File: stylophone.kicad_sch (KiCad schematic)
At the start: 8 parts, among them U1 LM555xM

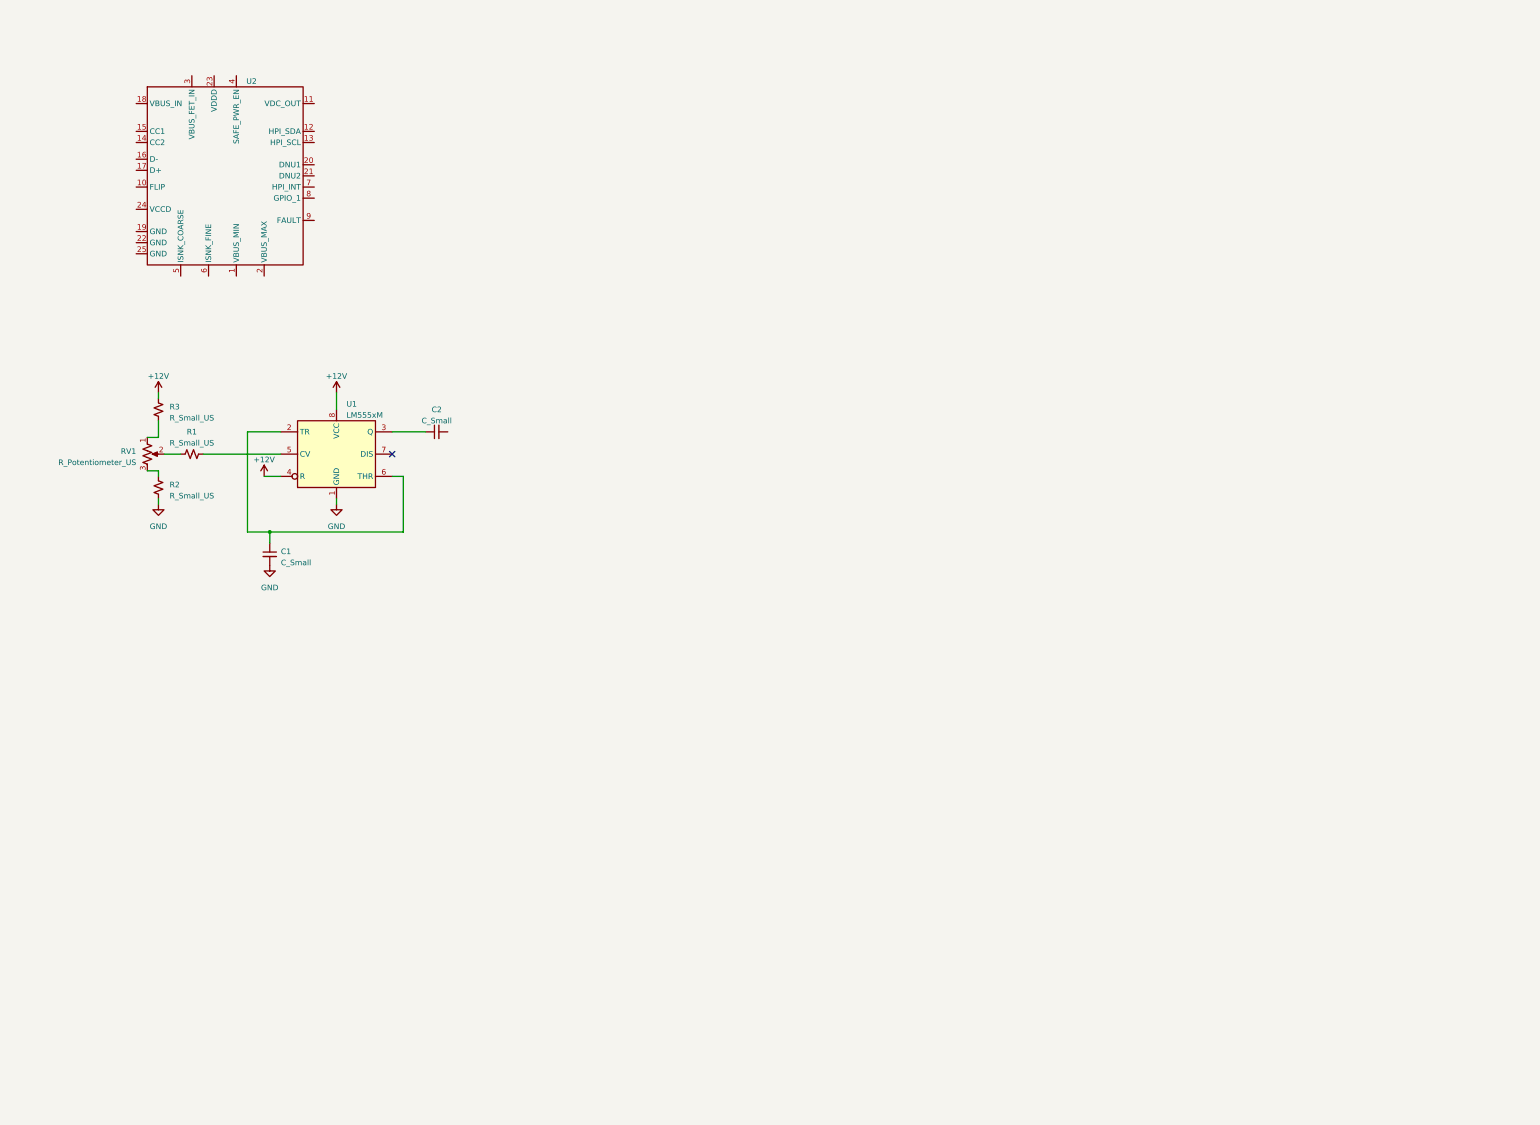
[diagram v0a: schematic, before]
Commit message: Updated all values and footprints
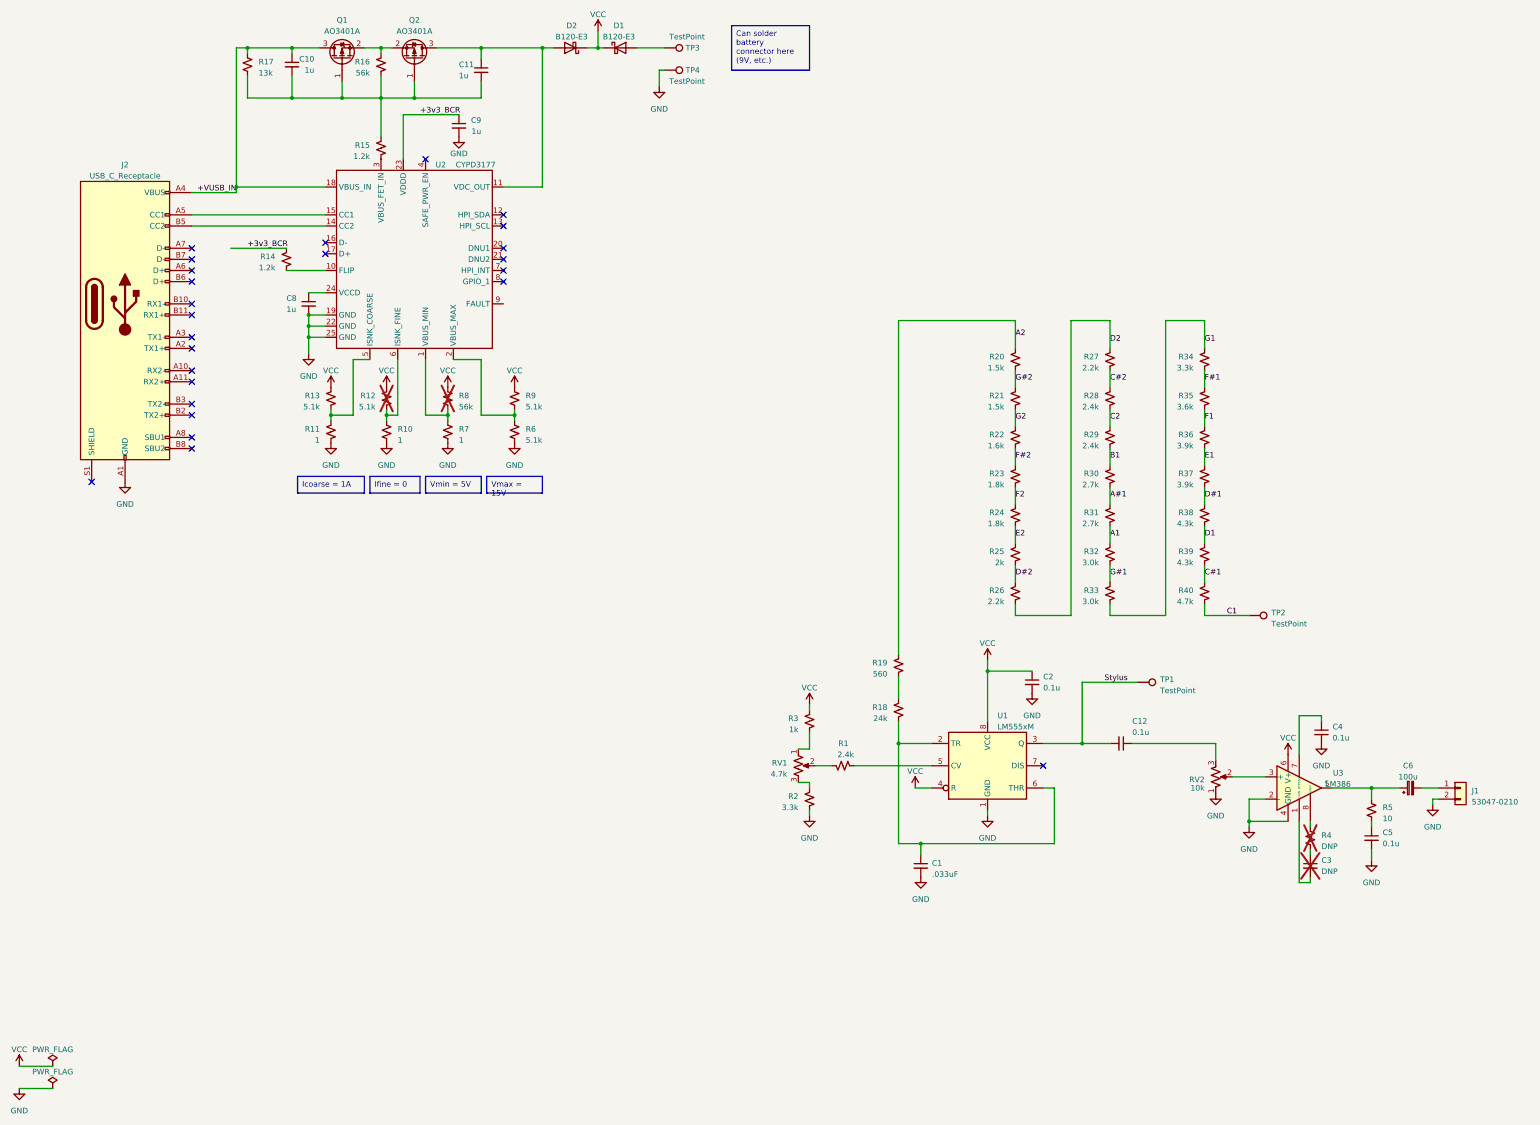
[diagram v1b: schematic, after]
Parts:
- added C10, C11, C8, C9: 1u, Capacitor_SMD:C_0603_1608Metric, symbol Device:C_Small
- added C12, C4, C5: 0.1u, Capacitor_SMD:C_0603_1608Metric, symbol Device:C_Small
- added C3: DNP, Capacitor_SMD:C_0603_1608Metric, symbol Device:C_Small
- added C6: 100u, Capacitor_SMD:CP_Elec_8x6.2, symbol Device:C_Polarized_Small
- added D1, D2: B120-E3, Diode_SMD:D_SMA, symbol Diode:B120-E3
- added J1: 53047-0210, Connector_Molex:Molex_PicoBlade_53047-0210_1x02_P1.25mm_Vertical, symbol Connector_Generic:Conn_01x02
- added J2: USB_C_Receptacle, Connector_USB:USB_C_Receptacle_Molex_105450-0101, symbol Connector:USB_C_Receptacle
- added Q1, Q2: AO3401A, Package_TO_SOT_SMD:SOT-23, symbol Transistor_FET:AO3401A
- added R10, R11, R7: 1, Resistor_SMD:R_0603_1608Metric, symbol Device:R_Small_US
- added R12, R13, R6, R9: 5.1k, Resistor_SMD:R_0603_1608Metric, symbol Device:R_Small_US
- added R14, R15: 1.2k, Resistor_SMD:R_0603_1608Metric, symbol Device:R_Small_US
- added R16, R8: 56k, Resistor_SMD:R_0603_1608Metric, symbol Device:R_Small_US
- added R17: 13k, Resistor_SMD:R_0603_1608Metric, symbol Device:R_Small_US
- added R18: 24k, Resistor_SMD:R_0603_1608Metric, symbol Device:R_Small_US
- added R19: 560, Resistor_SMD:R_0603_1608Metric, symbol Device:R_Small_US
- added R20, R21: 1.5k, Resistor_SMD:R_0603_1608Metric, symbol Device:R_Small_US
- added R22: 1.6k, Resistor_SMD:R_0603_1608Metric, symbol Device:R_Small_US
- added R23, R24: 1.8k, Resistor_SMD:R_0603_1608Metric, symbol Device:R_Small_US
- added R25: 2k, Resistor_SMD:R_0603_1608Metric, symbol Device:R_Small_US
- added R26, R27: 2.2k, Resistor_SMD:R_0603_1608Metric, symbol Device:R_Small_US
- added R28, R29: 2.4k, Resistor_SMD:R_0603_1608Metric, symbol Device:R_Small_US
- added R30, R31: 2.7k, Resistor_SMD:R_0603_1608Metric, symbol Device:R_Small_US
- added R32, R33: 3.0k, Resistor_SMD:R_0603_1608Metric, symbol Device:R_Small_US
- added R34: 3.3k, Resistor_SMD:R_0603_1608Metric, symbol Device:R_Small_US
- added R35: 3.6k, Resistor_SMD:R_0603_1608Metric, symbol Device:R_Small_US
- added R36, R37: 3.9k, Resistor_SMD:R_0603_1608Metric, symbol Device:R_Small_US
- added R38, R39: 4.3k, Resistor_SMD:R_0603_1608Metric, symbol Device:R_Small_US
- added R4: DNP, Resistor_SMD:R_0603_1608Metric, symbol Device:R_Small_US
- added R40: 4.7k, Resistor_SMD:R_0603_1608Metric, symbol Device:R_Small_US
- added R5: 10, Resistor_SMD:R_0603_1608Metric, symbol Device:R_Small_US
- added RV2: 10k, Potentiometer_THT:Potentiometer_Piher_T-16H_Single_Horizontal, symbol Device:R_Potentiometer_US
- added TP1, TP2, TP3, TP4: TestPoint, TestPoint:TestPoint_THTPad_D1.5mm_Drill0.7mm, symbol Connector:TestPoint
- added U3: LM386, Package_SO:SOIC-8_3.9x4.9mm_P1.27mm, symbol Amplifier_Audio:LM386
- C1: value C_Small -> .033uF
- C2: value C_Small -> 0.1u; footprint (none) -> Capacitor_SMD:C_0603_1608Metric
- R1: value R_Small_US -> 2.4k; footprint (none) -> Resistor_SMD:R_0603_1608Metric
- R2: value R_Small_US -> 3.3k; footprint (none) -> Resistor_SMD:R_0603_1608Metric
- R3: value R_Small_US -> 1k; footprint (none) -> Resistor_SMD:R_0603_1608Metric
- RV1: value R_Potentiometer_US -> 4.7k; footprint (none) -> Potentiometer_THT:Potentiometer_Piher_T-16H_Single_Horizontal
- U2: value ~ -> CYPD3177; footprint (none) -> Package_DFN_QFN:QFN-24-1EP_4x4mm_P0.5mm_EP2.15x2.15mm
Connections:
- net GND: now also C2.2, U2.19 (GND), U2.22 (GND), U2.25 (GND), C4.2, C5.2, C8.2, C9.2, J1.2 (Pin_2), J2.A1 (GND), J2.A12 (GND), J2.B1 (GND), J2.B12 (GND), R10.1, R11.1, R6.1, R7.1, RV2.1, TP4.1, U3.2 (-), U3.4 (GND)
- net at RV1.2: now also R1.2; no longer R1.1
- net at C1.1, U1.2 (TR), U1.6 (THR): now also R18.1
- net at U2.1 (VBUS_MIN): now also R7.2, R8.1
- net at U2.10 (FLIP): now also R14.1
- net at U2.11 (VDC_OUT): now also C11.1, D2.2 (A), Q2.3 (D)
- net at U2.14 (CC2): now also J2.B5 (CC2)
- net at U2.15 (CC1): now also J2.A5 (CC1)
- net +VUSB_IN: now reaches U2.18 (VBUS_IN)
- net +VUSB_IN: now also C10.1, J2.A4 (VBUS), J2.A9 (VBUS), J2.B4 (VBUS), J2.B9 (VBUS), Q1.3 (D), R17.2
- net at U2.2 (VBUS_MAX): now also R6.2, R9.1
- net +3v3_BCR: now reaches U2.23 (VDDD)
- net +3v3_BCR: now also C9.1, R14.2
- net at U2.24 (VCCD): now also C8.1
- net at U2.3 (VBUS_FET_IN): now also R15.1
- net at U2.5 (ISNK_COARSE): now also R11.2, R13.1
- net at U2.6 (ISNK_FINE): now also R10.2, R12.1
- net at U1.5 (CV): now also R1.1; no longer R1.2
- net Stylus: now reaches U1.3 (Q)
- net Stylus: now also C12.2, TP1.1; no longer C2.1
- net +12V renamed VCC
- net VCC: now also C2.1, D1.1 (K), D2.1 (K), R12.2, R13.2, R8.2, R9.2, U3.6 (V+)
- new net: C12.1, RV2.3
- new net: C3.1, R4.1
- new net: C3.2, U3.1 (GAIN)
- new net: D1.2 (A), TP3.1
- new net: C10.2, C11.2, Q1.1 (G), Q2.1 (G), R15.2, R16.1, R17.1
- new net: Q1.2 (S), Q2.2 (S), R16.2
- new net: R4.2, U3.8 (GAIN)
- new net: RV2.2, U3.3 (+)
- new net: C6.1, R5.2, U3.5
- new net: C4.1, U3.7 (BYPASS)
- new net: R18.2, R19.1
- new net: C5.1, R5.1
- new net: C6.2, J1.1 (Pin_1)
- new net A#1: R30.1, R31.2
- new net A1: R31.1, R32.2
- new net A2: R19.2, R20.2
- new net B1: R29.1, R30.2
- new net C#1: R39.1, R40.2
- new net C#2: R27.1, R28.2
- new net C1: R40.1, TP2.1
- new net C2: R28.1, R29.2
- new net D#1: R37.1, R38.2
- new net D#2: R25.1, R26.2
- new net D1: R38.1, R39.2
- new net D2: R26.1, R27.2
- new net E1: R36.1, R37.2
- new net E2: R24.1, R25.2
- new net F#1: R34.1, R35.2
- new net F#2: R22.1, R23.2
- new net F1: R35.1, R36.2
- new net F2: R23.1, R24.2
- new net G#1: R32.1, R33.2
- new net G#2: R20.1, R21.2
- new net G1: R33.1, R34.2
- new net G2: R21.1, R22.2
- no-connect marks 1 -> 25
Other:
- moved on the sheet: C1, RV1, U1, U2

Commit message: updated 3d models
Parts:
- C1: value .033uF -> .033u; footprint (none) -> Capacitor_SMD:C_0603_1608Metric
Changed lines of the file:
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@@
+    )
+  )
+  (symbol (lib_id "Device:C_Small") (at 227.33 219.71 0) (unit 1)
+    (in_bom yes) (on_board yes) (dnp no)
+    (property "Reference" "C1" (at 229.87 218.44 0)
+      (effects (font (size 1.27 1.27)) (justify left))
+    )
+    (property "Value" ".033u" (at 229.87 220.98 0)
+      (effects (font (size 1.27 1.27)) (justify left))
+    )
+    (property "Footprint" "Capacitor_SMD:C_0603_1608Metric" (at 227.33 219.71 0)
+      (effects (font (size 1.27 1.27)) hide)
+    )
+    (property "Datasheet" "~" (at 227.33 219.71 0)
+      (effects (font (size 1.27 1.27)) hide)
+    )
+    (pin "1")
+    (pin "2")
+    (instances
+      (project "stylophone"
+        (path "/af730536-f480-4276-b0c9-05391d212333"
+          (reference "C1") (unit 1)
+        )
+      )
     )
   )
@@
         )
       )
-    )
-  )
-  (symbol (lib_id "Device:C_Small") (at 227.33 219.71 0) (unit 1)
-    (in_bom yes) (on_board yes) (dnp no) (fields_autoplaced)
-    (property "Reference" "C1" (at 229.87 219.0813 0)
-      (effects (font (size 1.27 1.27)) (justify left))
-    )
-    (property "Value" ".033uF" (at 229.87 221.6213 0)
-      (effects (font (size 1.27 1.27)) (justify left))
-    )
-    (property "Footprint" "" (at 227.33 219.71 0)
-      (effects (font (size 1.27 1.27)) hide)
-    )
-    (property "Datasheet" "~" (at 227.33 219.71 0)
-      (effects (font (size 1.27 1.27)) hide)
-    )
-    (pin "1")
-    (pin "2")
-    (instances
-      (project "stylophone"
-        (path "/af730536-f480-4276-b0c9-05391d212333"
-          (reference "C1") (unit 1)
-        )
-      )
